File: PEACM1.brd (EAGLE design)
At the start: 91.7 x 48.7 mm, 26 parts, among them T1 MJ4502

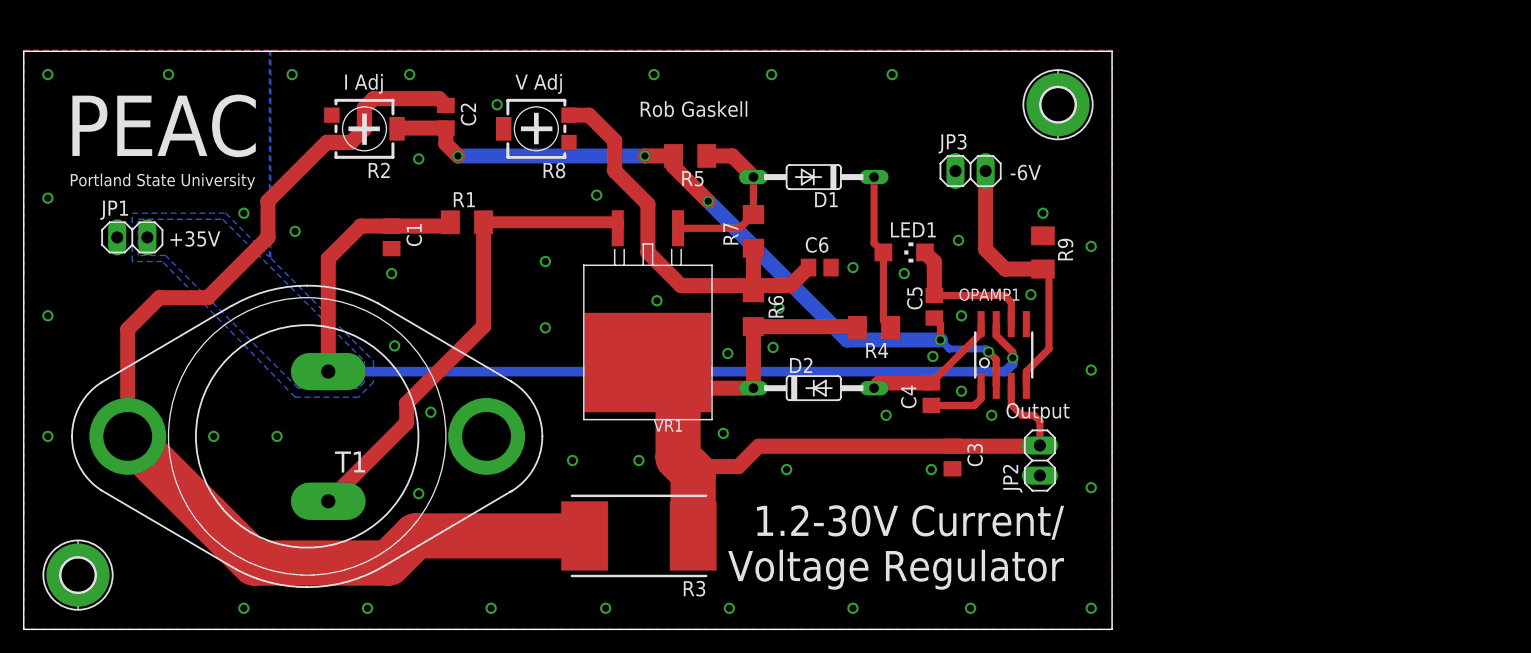
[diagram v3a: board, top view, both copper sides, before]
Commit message: Added -6V regulator, banana jacks.
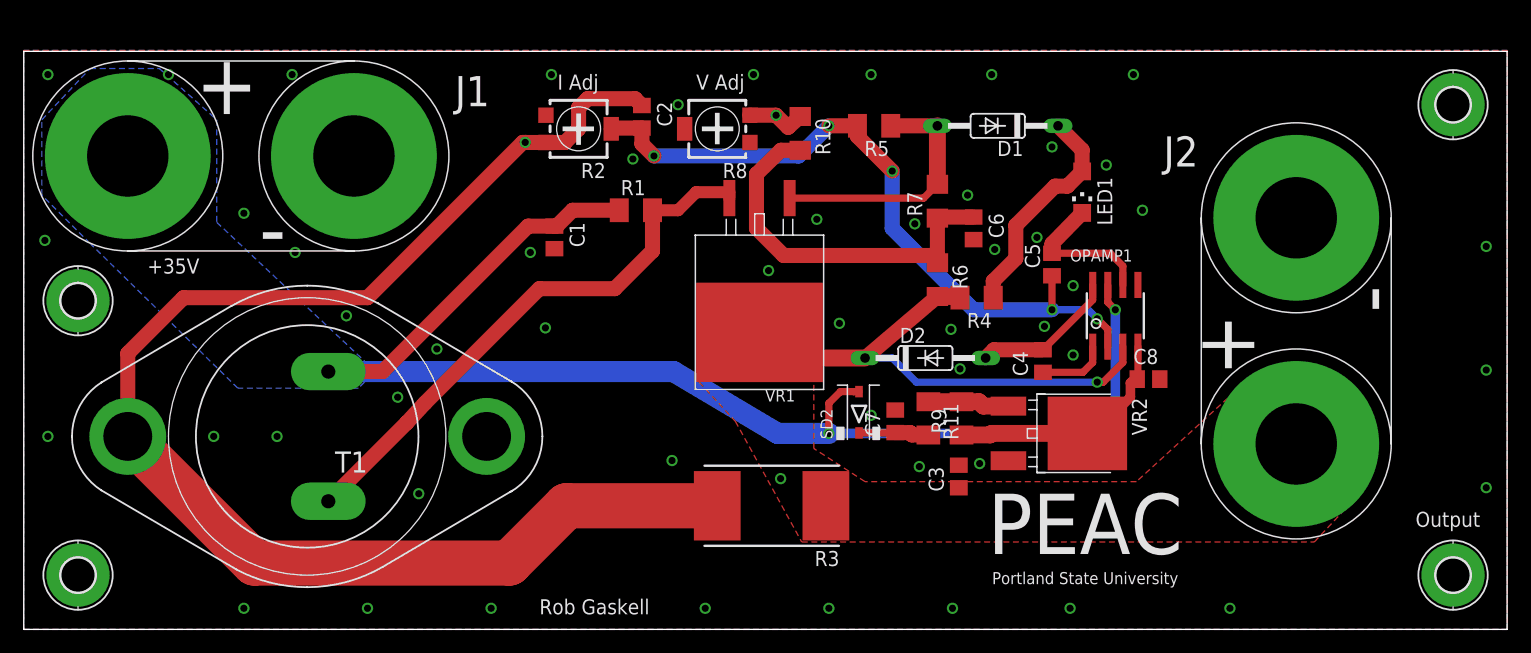
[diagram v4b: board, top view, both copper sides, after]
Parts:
- removed JP1, JP2, JP3: (no value), pinhead:1X02
- added C7, C8: 1u, rcl:C0805
- added H3, H4: MOUNT-PAD-ROUND2.8, holes:2,8-PAD
- added J1, J2: BU-P2269, PEAC:BU-P2269
- added R10: 10, rcl:R1206
- added R11: 33, rcl:M1206
- added SD2: STPS0540Z, motorFeedback:SOD-123
- added VR2: LM337, PEAC:DPAK(TO-252)
- R2: value (none) -> 250k
- R9: value NU -> 33
- moved H2 33.3 mm to (120.4, 44.2)
- moved R2 18.0 mm to (46.7, 42.2)
- moved C2 16.5 mm to (52.1, 43.2)
- moved D1 16.1 mm to (82.0, 42.4)
- moved LED1 15.8 mm to (89.2, 36.8), turned to 180 degrees
- moved R5 15.7 mm to (71.6, 42.4)
- moved R6 15.7 mm to (77.0, 29.5)
- moved R7 15.7 mm to (77.0, 36.1)
- moved R9 15.6 mm to (79.0, 17.8), turned to 90 degrees
- moved R8 15.2 mm to (58.4, 42.2)
- moved R1 14.3 mm to (51.6, 35.3)
- moved C1 13.7 mm to (44.7, 33.0)
- moved C6 13.4 mm to (80.0, 33.8), turned to 270 degrees
- moved R3 11.5 mm to (63.0, 10.4)
- moved C5 10.5 mm to (86.6, 30.7)
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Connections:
- net N$2 renamed EMITTER_RES
- new net N$2: C7.1, R11.2, SD2.C
- new net N$7: C6.1, R10.2, R6.1, R7.1
- new net SCH_RES_VCC-: R11.1, R9.2, VR2.GND
- net +1.2-30V: now also J2.+; no longer JP2.1
- net +35V: now also J1.+, SD2.A; no longer JP1.2
- net GND: now also C7.2, C8.2, H3.B2,8, H4.B2,8, J1.-, J2.-, VR2.INPUT; no longer JP1.1, JP2.2, JP3.1, R9.1
- net N$6: now also R10.1; no longer C6.1, R6.1, R7.1
- net VCC-: now also C8.1, R9.1, VR2.OUTPUT; no longer JP3.2, R9.2
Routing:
- net N$7: track 0.00 -> 32.1 mm
- net +35V: track 82.9 -> 114.5 mm, vias 1 -> 2
- net +1.2-30V: track 74.3 -> 44.3 mm, vias 0 -> 1
- net N$6: track 34.4 -> 5.02 mm
- net EMITTER_RES: track 90.8 -> 116.5 mm, vias 0 -> 1
- net N$5: track 14.7 -> 21.8 mm
- net SCH_RES_VCC-: track 0.00 -> 6.90 mm
- net N$3: track 40.7 -> 47.1 mm
- net N$2: track 0.00 -> 5.99 mm
- net N$8: track 13.3 -> 19.1 mm
- net N$4: track 64.1 -> 59.4 mm
- net VCC-: track 23.0 -> 20.1 mm
- net N$9: track 11.7 -> 12.3 mm
- added copper zone on layer 1, net +1.2-30V
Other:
- board size 91.7 x 48.7 mm -> 124.9 x 48.7 mm
- board text removed: "-6V"
